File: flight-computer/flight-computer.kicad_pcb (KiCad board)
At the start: 2 copper layers, 25.4 x 51.5 mm, 31 parts, among them J1 USB_C_Receptacle_USB2.0_16P, J3 Conn_01x02_Pin, J4 Conn_01x06_Pin, J5 Conn_01x06_Pin, J6 Power Connector, J7 Micro_SD_Card, Q1 DMN3404L, Q2 DMN3404L, SW1 Reset, SW2 Boot, U1 LMR51420X, U2 ESP32-S3-WROOM-1, U3 LSM6DSO32TR

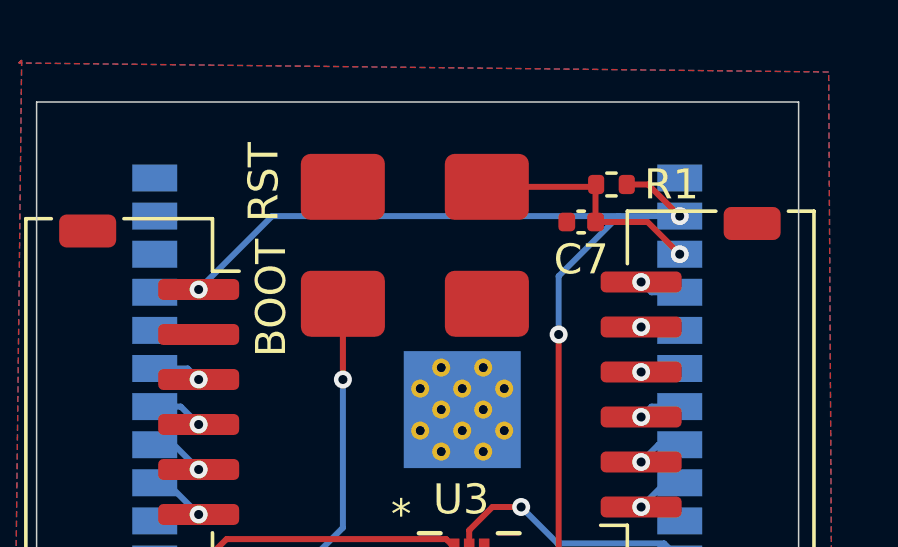
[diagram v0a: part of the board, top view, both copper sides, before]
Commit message: Fix button footprints
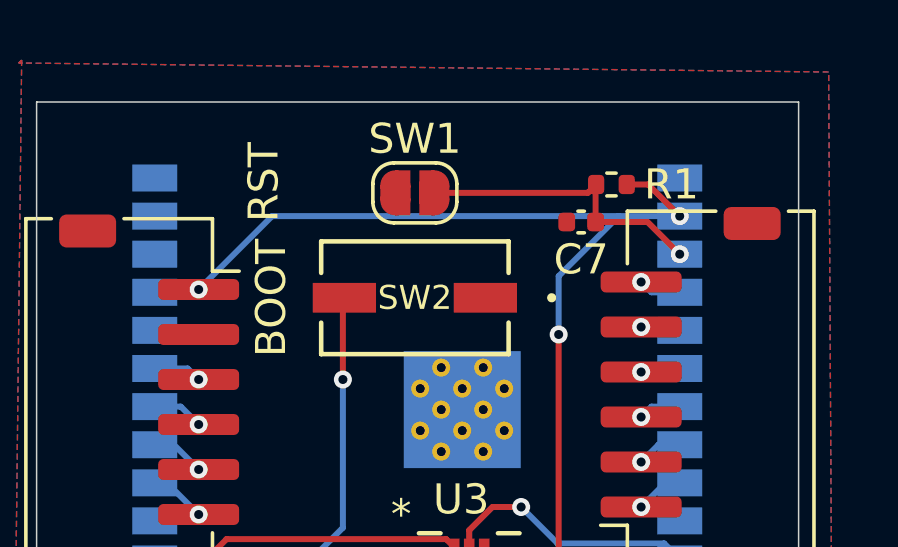
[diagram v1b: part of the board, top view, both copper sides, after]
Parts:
- SW1: footprint Library:FSM2JMTR -> Jumper:SolderJumper-2_P1.3mm_Open_RoundedPad1.0x1.5mm
- SW2: footprint Library:FSM2JMTR -> Library:SW_FSM2JMTR_TEC
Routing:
- net Net-(U2-EN): track 8.19 -> 10.0 mm

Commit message: add decoupling cap right next to esp32
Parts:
- added C5: 100nF, Capacitor_SMD:C_0402_1005Metric, B.Cu at (155.6, 82.0)
- C3: renamed from C7; value 1uF -> 100nF
- R1: value 10k -> 100k
- renumbered C3 to C4, C4 to C6, C5 to C7, C6 to C8, J5 to J1, J4 to J2, J6 to J3, J7 to J4, J1 to J5, J3 to J6, R5 to R4, R6 to R5
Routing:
- net GND: track 7.22 -> 9.37 mm
- net +3.3V: track 71.0 -> 73.1 mm

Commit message: finishing(?) touches on flight computer board
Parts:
- removed SW1: Reset, Jumper:SolderJumper-2_P1.3mm_Open_RoundedPad1.0x1.5mm
- removed SW2: Boot, Library:SW_FSM2JMTR_TEC
- added SW3: SW_DIP_x02, Library:218-2LPSTR_CTS, F.Cu at (143.8, 82.4)
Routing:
- net Net-(U2-IO0): track 15.7 -> 20.8 mm
- net Net-(U2-EN): track 10.0 -> 7.52 mm
- net GND: track 9.37 -> 7.70 mm
- net Net-(D1-A): track 13.4 -> 14.7 mm

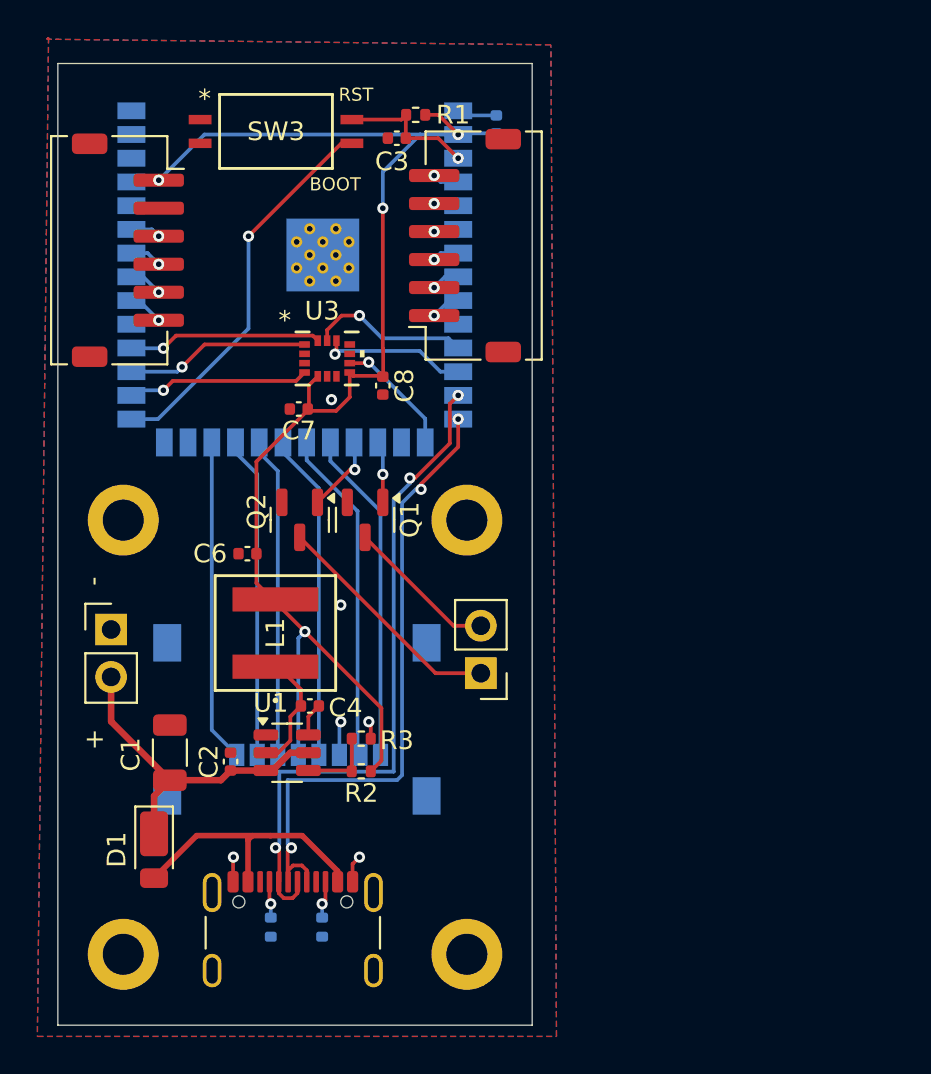
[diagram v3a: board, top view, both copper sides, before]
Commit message: added current sensor stuff and rerouted fc
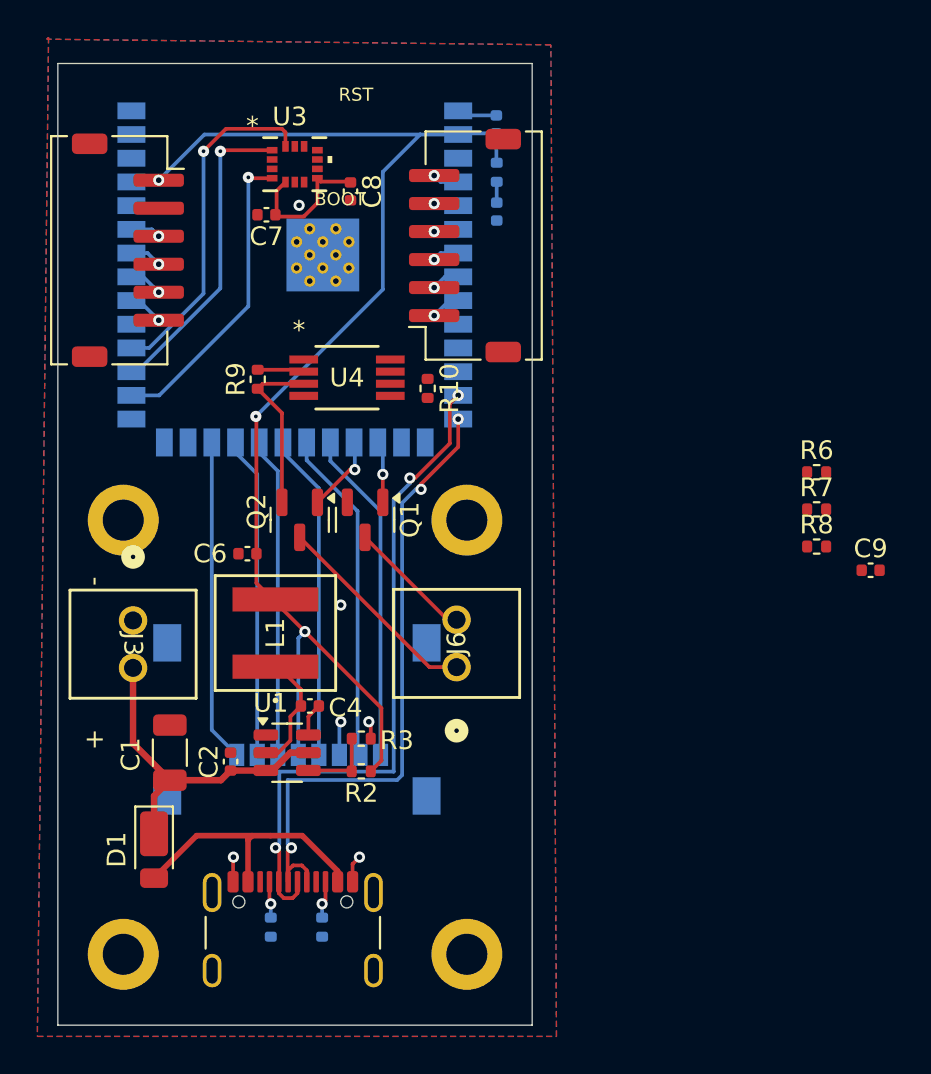
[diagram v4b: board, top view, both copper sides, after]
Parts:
- removed SW3: SW_DIP_x02, Library:218-2LPSTR_CTS
- added C9: 0.1uF, Capacitor_SMD:C_0402_1005Metric, F.Cu at (175.6, 105.9)
- added R10: 100 mOhm, Resistor_SMD:R_0402_1005Metric, F.Cu at (151.9, 96.1)
- added R6: 200 Ohm, Resistor_SMD:R_0402_1005Metric, F.Cu at (172.7, 100.6)
- added R7: 200 Ohm, Resistor_SMD:R_0402_1005Metric, F.Cu at (172.7, 102.6)
- added R8: 200 Ohm, Resistor_SMD:R_0402_1005Metric, F.Cu at (172.7, 104.6)
- added R9: 100 mOhm, Resistor_SMD:R_0402_1005Metric, F.Cu at (142.8, 95.7)
- added U4: INA2180A1IDGKR, Library:DGK8_TEX-M, F.Cu at (147.6, 95.6)
- C3, R1: moved to B.Cu
- J3, J6: footprint Connector_PinHeader_2.54mm:PinHeader_1x02_P2.54mm_Vertical -> Library:CONN2_282834-2_TEC
- moved C7 10.5 mm to (143.2, 86.8)
- moved C8 10.5 mm to (147.7, 85.6)
- moved U3 10.5 mm to (144.8, 84.1)
- moved C3 6.64 mm to (155.6, 86.7), turned to -90 degrees
- moved R1 5.32 mm to (155.6, 84.6), turned to -90 degrees
- moved J6 1.34 mm to (153.4, 111.1), turned to 90 degrees
- moved J3 1.27 mm to (136.1, 108.6), turned to -90 degrees
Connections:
- J1 pad 4: FIN_MOSI -> Net-(J1-Pin_4)
- J1 pad 6: FIN_SCK -> Net-(J1-Pin_6)
- J2 pad 2: FIN_CLK -> Net-(J2-Pin_2)
- Q1 pad 1: Remote Start 1 -> Net-(Q1-G)
- Q2 pad 1: Remote Start 2 -> Net-(Q2-G)
- U2 pad 27: Net-(U2-IO0) -> unconnected-(U2-IO0-Pad27)
- U2 pad 38: unconnected-(U2-IO2-Pad38) -> IMP_OUT2
- U2 pad 39: unconnected-(U2-IO1-Pad39) -> IMP_OUT1
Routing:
- net Net-(U2-IO0): track 20.8 -> 0.00 mm, vias 1 -> 0
- net (no net): track 0.00 -> 9.19 mm
- net LSM_SCK: track 8.62 -> 0.00 mm, vias 1 -> 0
- net LSM_MOSI: track 10.4 -> 18.6 mm
- net LSM_CS: track 7.88 -> 0.00 mm, vias 1 -> 0
- net LSM_INT1: track 9.78 -> 16.8 mm
- net LSM_MISO: track 9.88 -> 16.8 mm
- net LSM_INT2: track 6.59 -> 0.00 mm, vias 1 -> 0
- net Net-(U2-EN): track 7.52 -> 1.12 mm, vias 1 -> 0
- net +3.3V: track 73.1 -> 76.4 mm, vias 4 -> 3
- net Remote Start 2: track 4.20 -> 6.70 mm
- net Net-(J6-Pin_1): track 12.7 -> 11.3 mm
- net Net-(J6-Pin_2): track 8.16 -> 6.73 mm
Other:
- board text added: "fix me"

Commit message: finished connecting things
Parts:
- added R11: 200 Ohm, Resistor_SMD:R_0402_1005Metric, B.Cu at (133.9, 90.0)
- added R12: 200 Ohm, Resistor_SMD:R_0402_1005Metric, B.Cu at (155.7, 85.4)
- added R13: 200 Ohm, Resistor_SMD:R_0402_1005Metric, B.Cu at (155.7, 86.8)
- added R14: 200 Ohm, Resistor_SMD:R_0402_1005Metric, B.Cu at (155.7, 88.3)
- added R15: 200 Ohm, Resistor_SMD:R_0402_1005Metric, B.Cu at (155.7, 89.7)
- J1, J2: footprint Connector_JST:JST_ZH_S6B-ZR-SM4A-TF_1x06-1MP_P1.50mm_Horizontal -> Connector_JST:JST_ZE_SM06B-ZESS-TB_1x06-1MP_P1.50mm_Horizontal
- R10, R9: footprint Resistor_SMD:R_0402_1005Metric -> Resistor_SMD:R_1206_3216Metric
- R6, R7, R8: moved to B.Cu
- moved R7 41.2 mm to (133.9, 88.8)
- moved R6 39.8 mm to (133.8, 92.3)
- moved C9 30.3 mm to (147.0, 95.8)
- moved R8 21.7 mm to (155.7, 91.1), turned to 180 degrees
- moved R9 13.1 mm to (148.4, 107.5)
- moved R10 10.4 mm to (151.0, 106.5)
- moved U4 3.51 mm to (145.2, 98.1)
- moved C3 2.99 mm to (156.2, 83.7)
- moved J1 2.77 mm to (136.9, 91.3)
- moved R1 2.73 mm to (155.7, 81.8), turned to 0 degrees
- moved C5 1.56 mm to (155.7, 80.4), turned to 180 degrees
- moved J2 1.22 mm to (152.7, 88.5)
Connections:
- C9 pad 2: unconnected-(C9-Pad2) -> +3.3V
- J1 pad 5: FIN_MISO -> Net-(J1-Pin_5)
- J2 pad 3: FIN_CS4 -> Net-(J2-Pin_3)
- J2 pad 4: FIN_CS3 -> Net-(J2-Pin_4)
- J2 pad 5: FIN_CS2 -> Net-(J2-Pin_5)
- J2 pad 6: FIN_CS1 -> Net-(J2-Pin_6)
- Q1 pad 1: Net-(Q1-G) -> Remote Start 1
- Q1 pad 3: Net-(J6-Pin_2) -> Net-(Q1-D)
- Q2 pad 1: Net-(Q2-G) -> Remote Start 2
- Q2 pad 3: Net-(J6-Pin_1) -> Net-(Q2-D)
- R10 pad 1: Remote Start 1 -> Net-(Q1-D)
- R10 pad 2: Net-(Q1-G) -> Net-(J6-Pin_2)
- R9 pad 1: Net-(Q2-G) -> Net-(J6-Pin_1)
- R9 pad 2: Remote Start 2 -> Net-(Q2-D)
- U4 pad 2: Net-(Q2-G) -> Net-(Q2-D)
- U4 pad 3: Remote Start 2 -> Net-(J6-Pin_1)
- U4 pad 5: Remote Start 1 -> Net-(J6-Pin_2)
- U4 pad 6: Net-(Q1-G) -> Net-(Q1-D)
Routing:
- net LSM_SCK: track 0.00 -> 23.3 mm, vias 0 -> 3
- net LSM_CS: track 0.00 -> 22.0 mm, vias 0 -> 3
- net IMP_OUT2: track 0.00 -> 21.9 mm, vias 0 -> 1
- net LSM_INT2: track 0.00 -> 20.4 mm, vias 0 -> 3
- net IMP_OUT1: track 0.00 -> 18.8 mm, vias 0 -> 1
- net +3.3V: track 76.4 -> 88.8 mm, vias 3 -> 5
- net Net-(Q2-D): track 0.00 -> 11.9 mm
- net Net-(Q1-D): track 0.00 -> 11.5 mm
- net Net-(J6-Pin_1): track 11.3 -> 21.5 mm
- net (no net): track 9.19 -> 0.00 mm
- net Net-(J1-Pin_4): track 0.00 -> 8.99 mm, vias 0 -> 1
- net Net-(J1-Pin_5): track 0.00 -> 8.14 mm, vias 0 -> 1
- net Net-(J6-Pin_2): track 6.73 -> 14.8 mm
- net Net-(J1-Pin_6): track 0.00 -> 7.97 mm, vias 0 -> 1
- net Net-(J2-Pin_2): track 0.00 -> 7.68 mm, vias 0 -> 1
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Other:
- board text added: "ew please fix"

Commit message: fixed?
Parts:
- moved J6 2.68 mm to (154.3, 113.6)
- moved C9 0.50 mm to (147.0, 95.3)
- moved C8 0.47 mm to (147.3, 85.6)
- moved C7 0.43 mm to (143.7, 86.8)
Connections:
- J2 pad MP: (no net) -> GND
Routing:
- net +3.3V: track 88.8 -> 27.0 mm, vias 5 -> 9
- net Net-(J6-Pin_1): track 21.5 -> 27.8 mm
- net USB_D+: track 34.8 -> 32.4 mm
- net USB_D-: track 36.4 -> 34.1 mm
- net Net-(J6-Pin_2): track 14.8 -> 17.0 mm
- net GND: vias 8 -> 10
- added copper zone on In2.Cu, net +3.3V
- added copper zone on In3.Cu, net +3.3V
- added copper zone on In1.Cu, net GND
- added copper zone on In4.Cu, net GND
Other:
- copper layers 2 -> 6

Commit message: small fixups
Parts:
- moved C6 0.67 mm to (142.7, 104.6)
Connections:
- J2 pad MP: GND -> (no net)
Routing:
- net +3.3V: track 27.0 -> 25.0 mm
- net LSM_CS: track 22.0 -> 20.1 mm, vias 3 -> 1
- net LSM_INT2: track 20.4 -> 18.6 mm, vias 3 -> 1
- net Net-(J6-Pin_2): track 17.0 -> 17.6 mm
- net LSM_SCK: track 23.3 -> 23.4 mm, vias 3 -> 1
- net GND: vias 10 -> 23
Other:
- board text added: "BR"
- board text added: "Live Video"
- board text removed: "BOOT"
- board text removed: "RST"
- board text removed: "ew please fix"

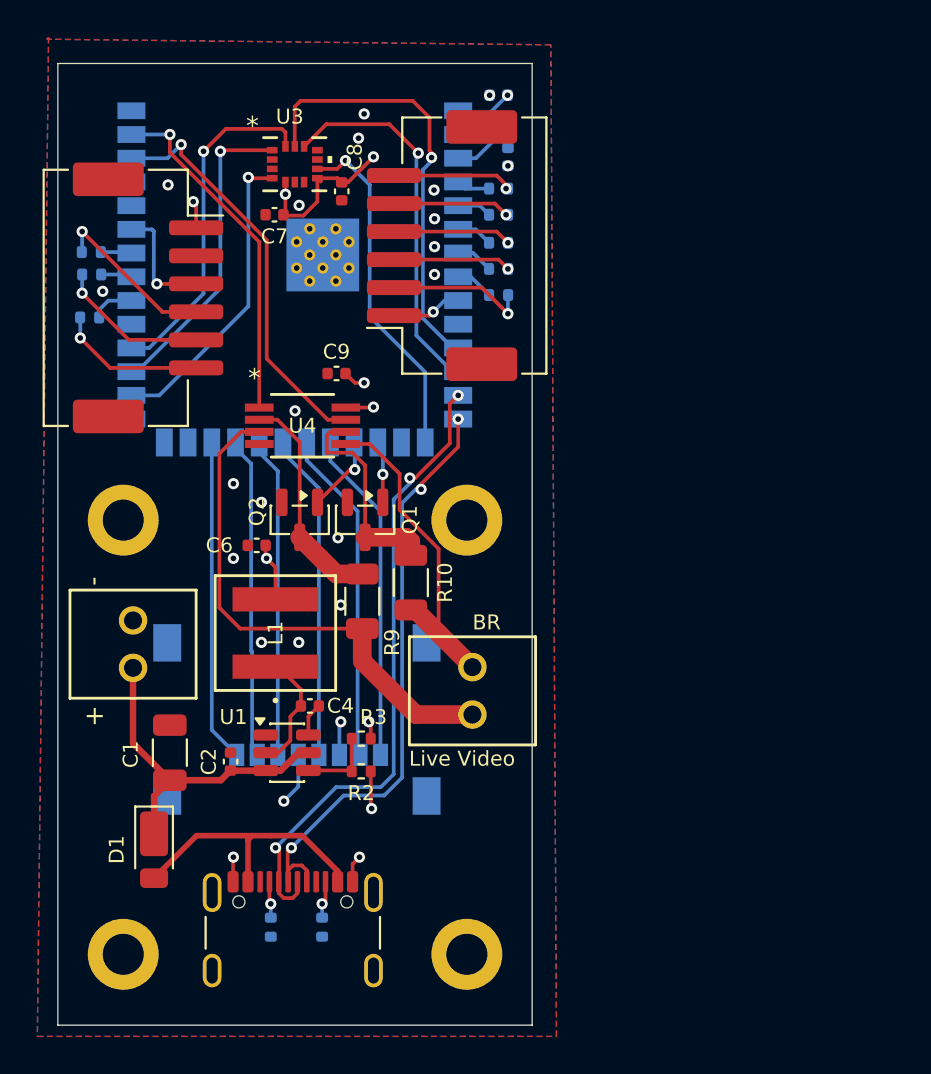
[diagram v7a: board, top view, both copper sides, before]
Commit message: make board 4 layers instead of 6
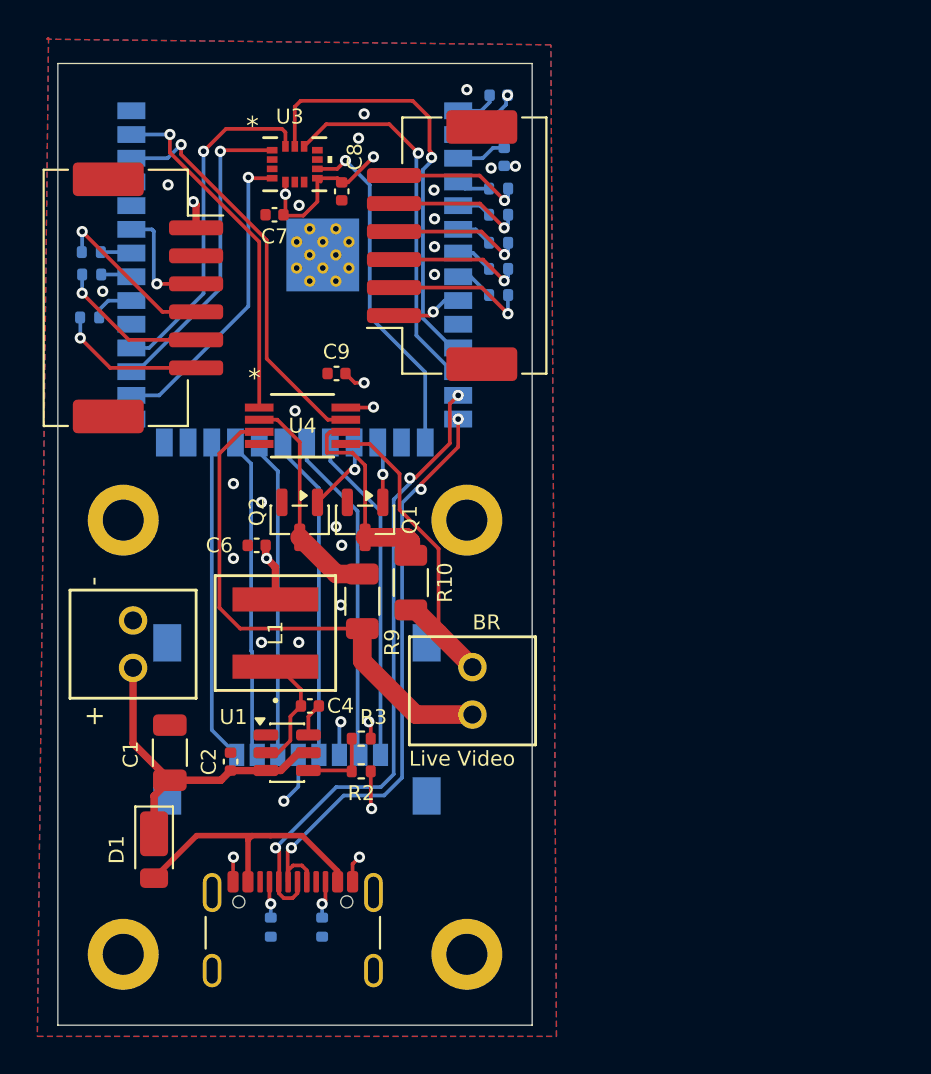
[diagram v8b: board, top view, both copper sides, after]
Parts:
- moved C3 0.20 mm to (156.0, 83.7)
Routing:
- net GND: track 5.55 -> 7.81 mm, vias 23 -> 25
- net Net-(J2-Pin_5): track 6.25 -> 7.23 mm
- net Net-(U2-EN): track 5.06 -> 4.20 mm
- net Net-(J2-Pin_4): track 6.35 -> 7.14 mm
- net Net-(J2-Pin_3): track 6.31 -> 7.09 mm
- net Net-(J2-Pin_6): track 6.41 -> 7.18 mm
- removed copper zone on In3.Cu, net +3.3V
- removed copper zone on In4.Cu, net GND
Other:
- copper layers 6 -> 4
